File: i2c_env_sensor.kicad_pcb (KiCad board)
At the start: 2 copper layers, 18 x 40 mm, 19 parts, among them J1 PH_4P_Header_3V3_I2C, U1 SHT40-AD1B-R3, U2 LPS22HBTR, U3 OPT3001DNPR

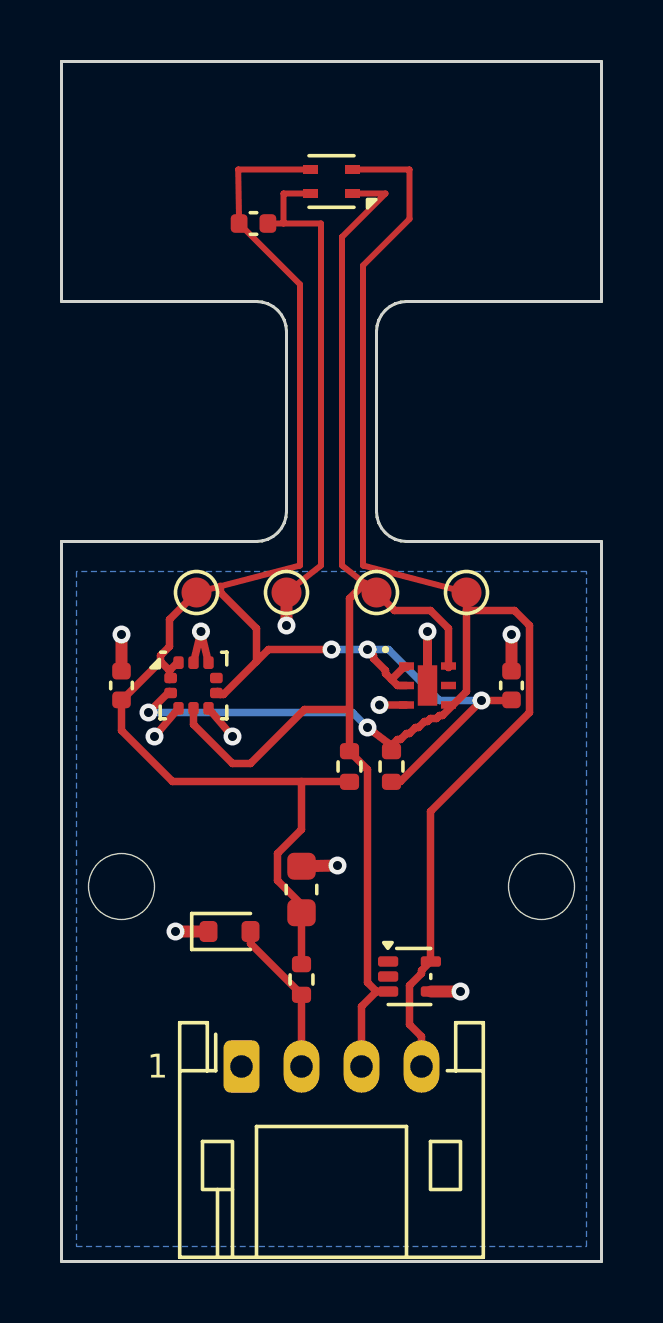
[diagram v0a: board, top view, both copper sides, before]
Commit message: Move the rail TVS to the cheaper package of the same part
TPD1E10B06 in TI's X1SON-2 (DPY) rather than SOT-5X3 (DYA): the same
die and the same datasheet, at $0.042 against $0.116 in ones, and 95,921
in stock against 8,682. The land pattern is DPY0002A read from the
datasheet already in evidence - two 0.3 x 0.5 mm pads 0.7 mm apart - and
the part now carries its own symbol, because the generic TVS symbol's
footprint filters are written for through-hole diode packages and pairing
them with this land pattern reads as a parity mismatch.

Checked every part against its manufacturer while here. TI publishes
Active/Production for all three of its parts in the package addenda dated
2025-2026, and Sensirion's catalogue reports SHT40 active; ST is not
reachable from this machine, so LPS22HB's status is unestablished rather
than confirmed. JLCPCB carries all ten, buyable, none idle or blacklisted.

$4.2084 to $4.1677 per board at 500.

Co-Authored-By: Claude Opus 5 <noreply@anthropic.com>
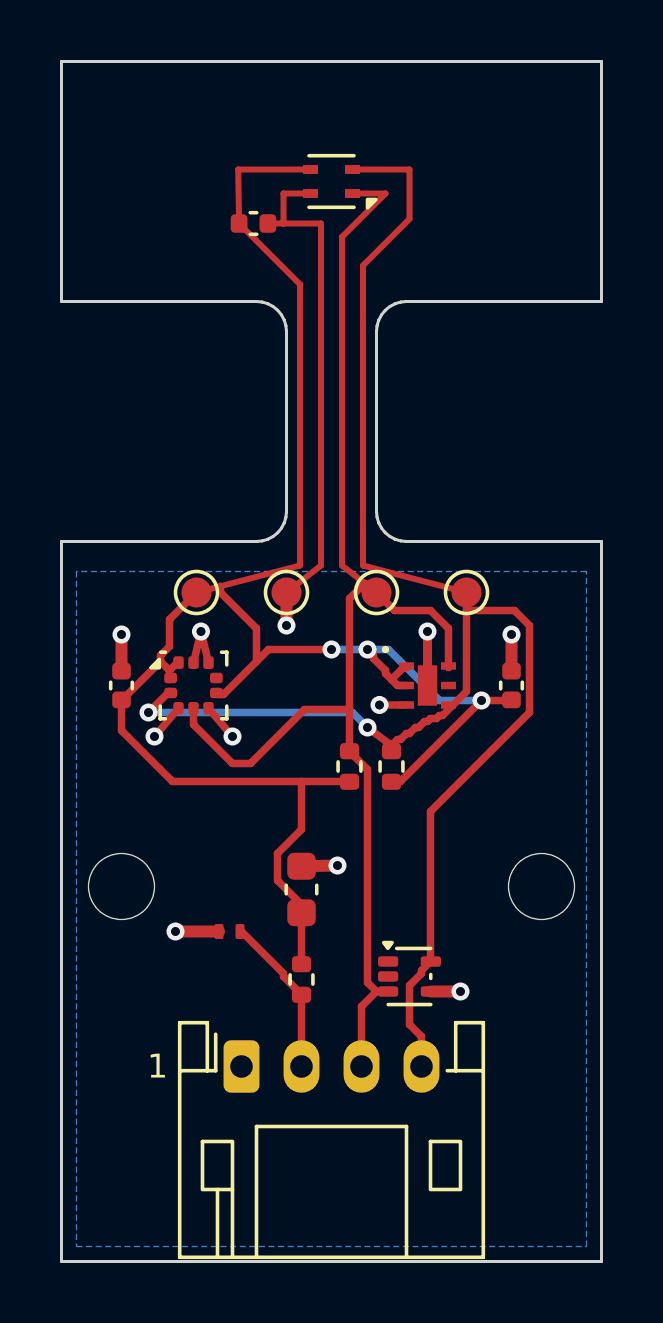
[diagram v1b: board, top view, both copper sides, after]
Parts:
- D2: value TPD1E10B06DYAR -> TPD1E10B06DPYR; footprint Diode_SMD:D_SOD-523 -> EnvSensorPod:Texas_X1SON-2_1.1x0.7mm_P0.7mm

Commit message: Complete the first owned routing cycle: search, replay, adopt, proven
The re-review demanded a real consumer run the toolkit's owned loop
end to end. This board did, against the real pinned router:

- The first search refused all three candidates honestly -
  ROUTE.TINY_SEGMENTS named 11 sub-floor fragments the declared
  transform list did not fold.
- The declaration widened (snap_to_pad_anchor, fold_subfloor, dedupe,
  trim_dangling_ends added); `route --replay` re-judged the recorded
  candidates through the changed transforms without re-searching, and
  attempt 2 was accepted and adopted, digest-verified.
- A fresh search->accept->adopt then completed in one run from the
  regenerated pre-route board; the record carries the honest 1/2
  accept rate (the pinned router is not run-to-run deterministic).
- `route --check` now prints OK with the complete resolved plan
  proven against the installed record - the first fully-proven board.

The routing record test re-points from the legacy `generated_nets`
field to the owned record's claims (GND reserved and spliced, the
plan digest bound); the neck-lane geometry stays proven on the board
itself. placement.courtyard is declared (edge clearance is not: J1
is an edge connector by design). The `design/route.py` invoker is
deleted per the plan - `run.py route` is the entry - and the tests
read endpoints through pcbqa.board.

Co-Authored-By: Claude Fable 5 <noreply@anthropic.com>
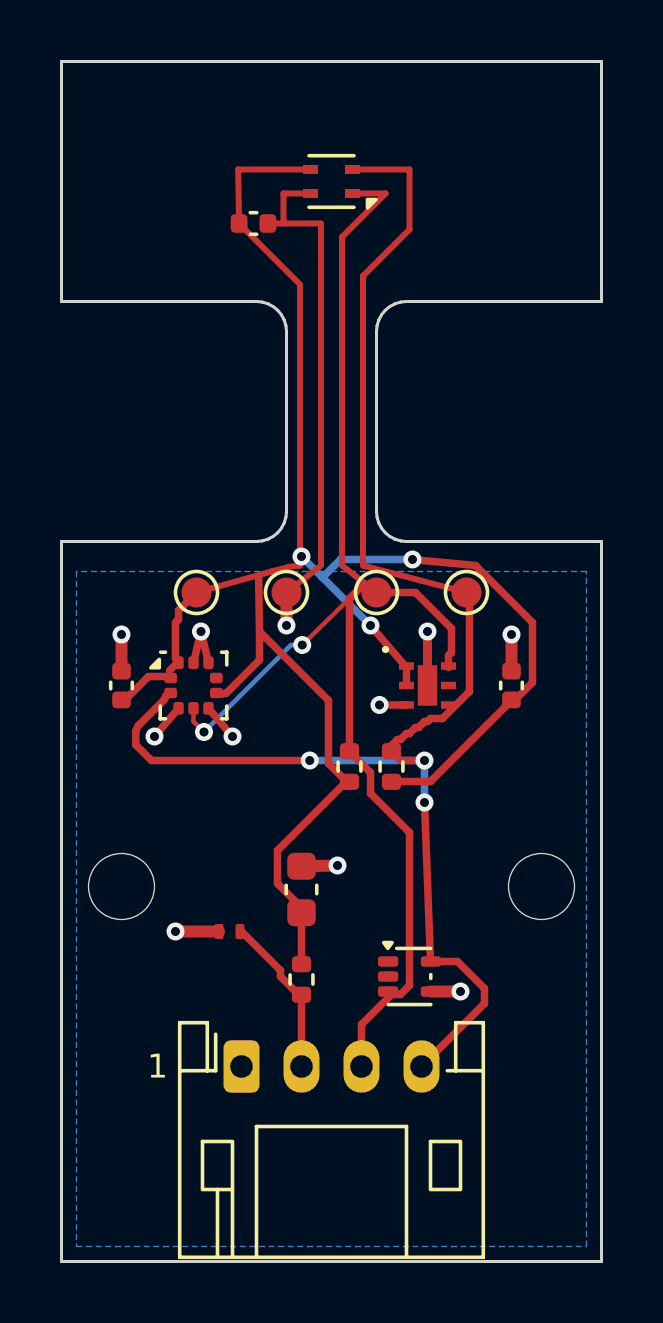
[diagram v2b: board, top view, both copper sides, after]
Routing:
- net SCL: track 54.4 -> 51.7 mm, vias 2 -> 3
- net 3V3: track 63.0 -> 65.7 mm
- net SDA: track 44.1 -> 45.6 mm, vias 0 -> 2
